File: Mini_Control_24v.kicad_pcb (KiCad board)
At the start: 2 copper layers, 130 x 100 mm, 60 parts, among them J1 Screw_Terminal_01x02, J2 Screw_Terminal_01x04, J3 Screw_Terminal_01x04, J4 Screw_Terminal_01x03, J5 Screw_Terminal_01x03, J6 ВН-20, J7 USB_B_Micro, J8 Screw_Terminal_01x02, K1 G2RL-1, K2 G2RL-1, U1 STM32F051C8Tx, U2 ISO1212, U3 ISO1212, U4 MAX3485, U5 USBLC6-2SC6, U6 FT232RL, U7 LM2596S-3.3, U8 ULN2003A

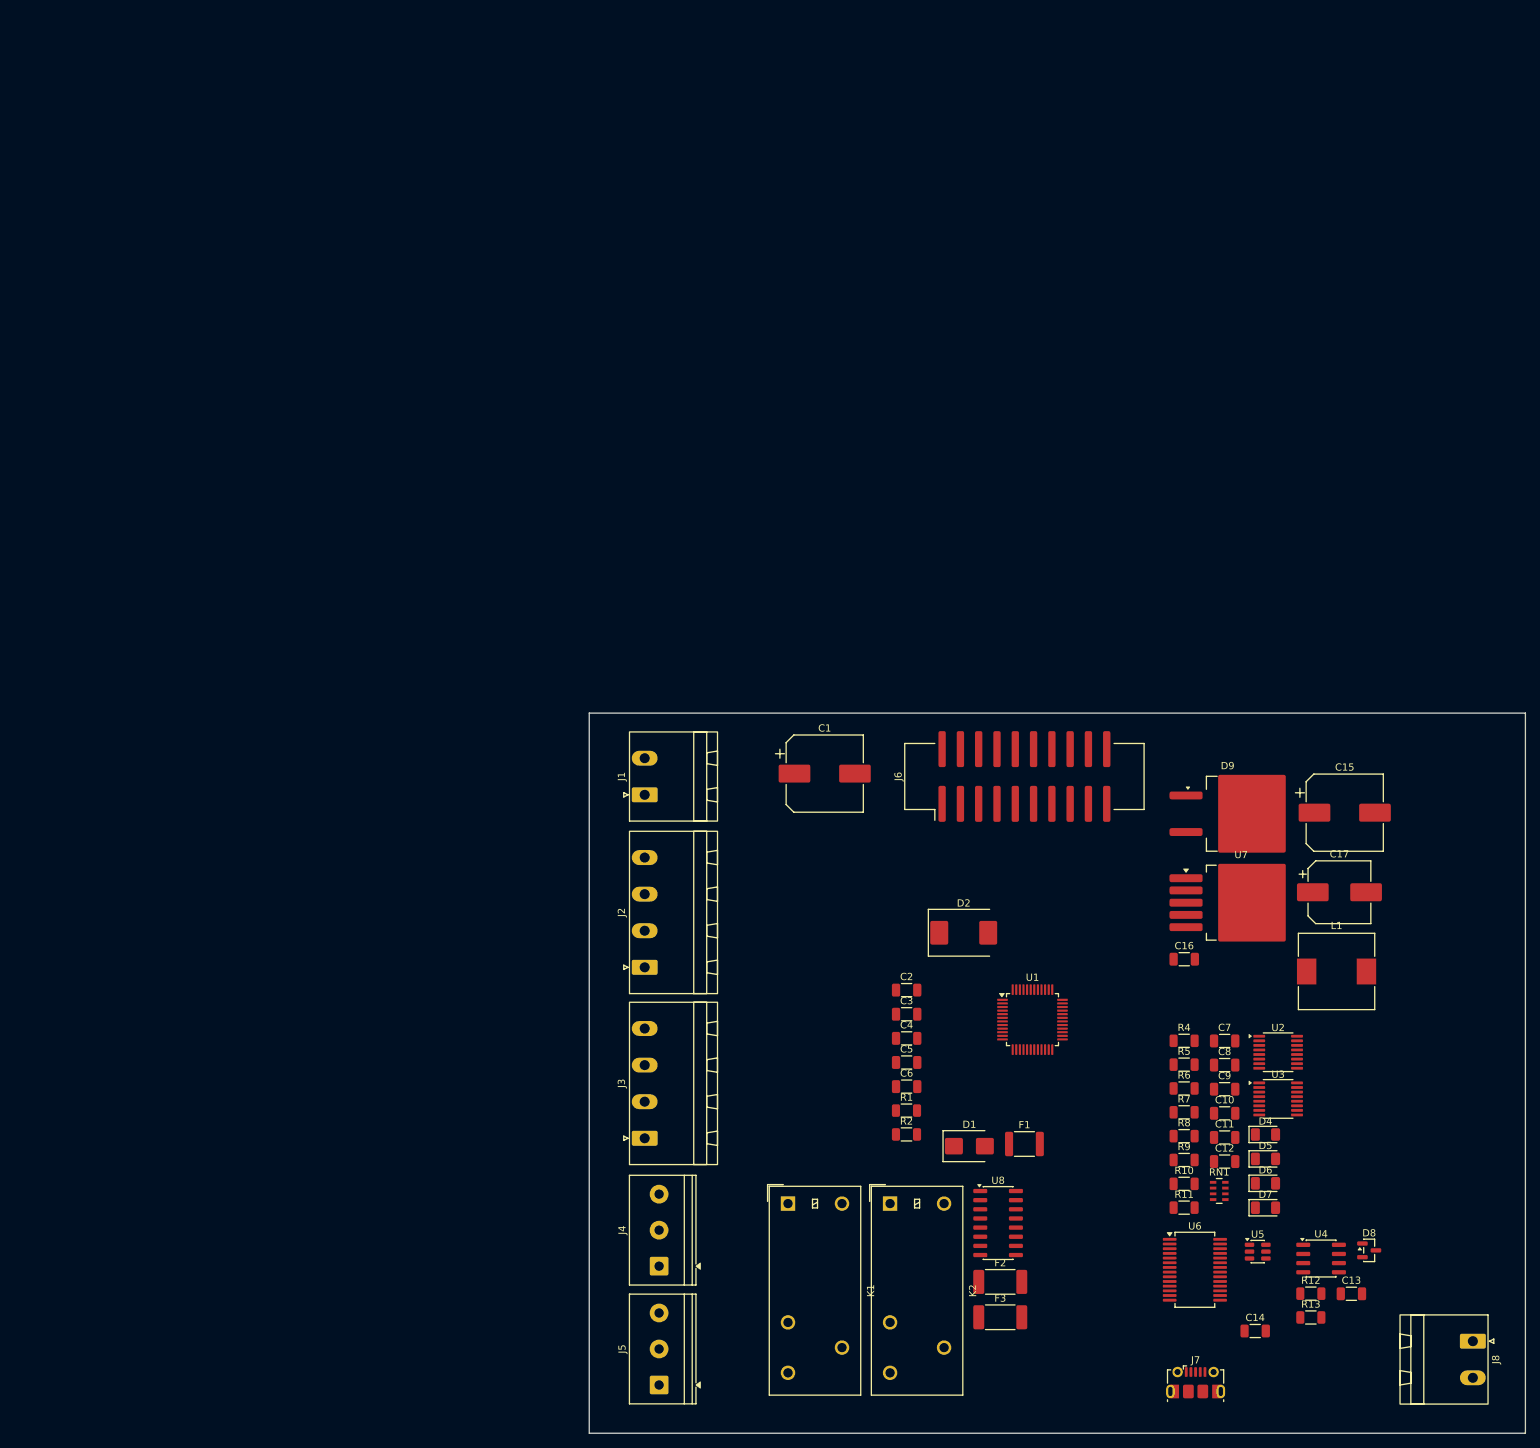
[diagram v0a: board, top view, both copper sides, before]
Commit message: Трассировка питания и цифровых входов-выходов
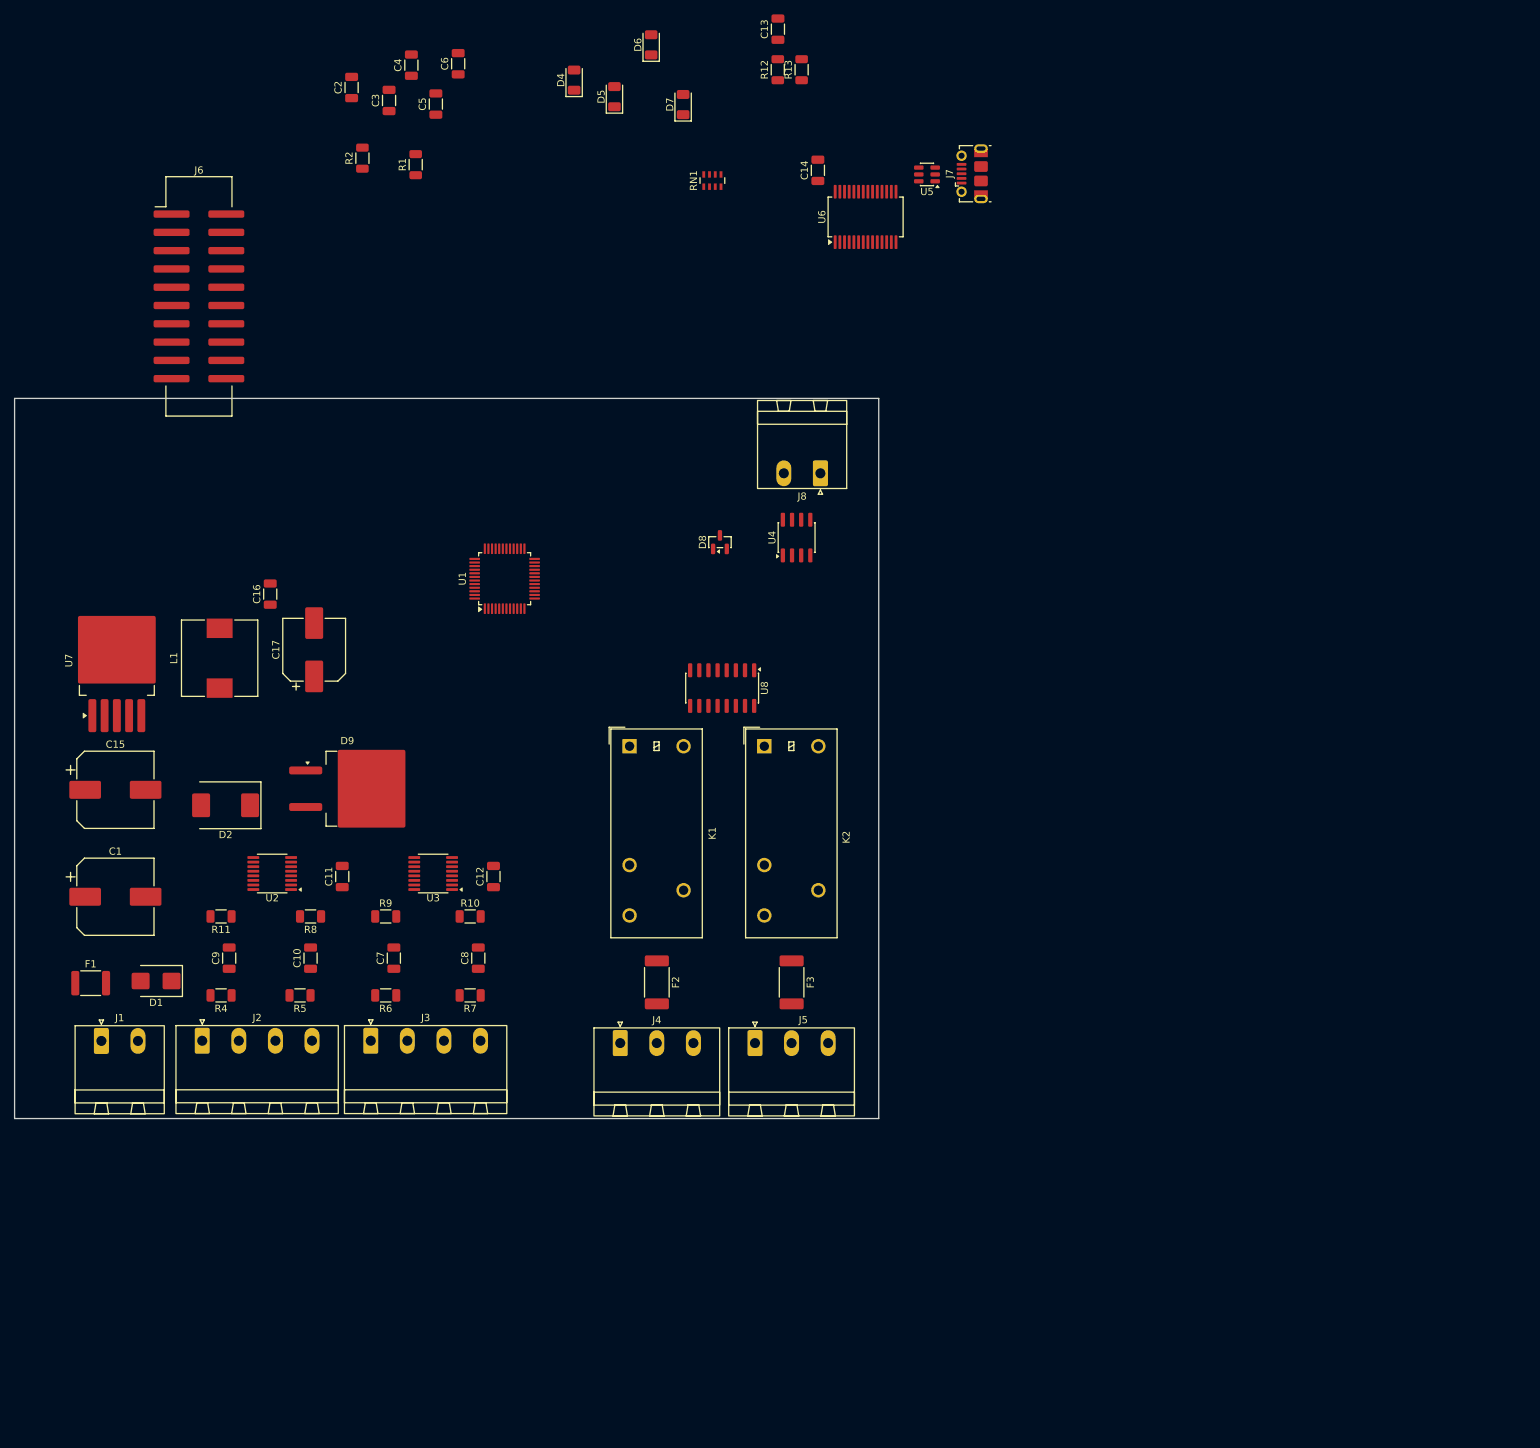
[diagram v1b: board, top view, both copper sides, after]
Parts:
- J4, J5: footprint TerminalBlock_Phoenix:TerminalBlock_Phoenix_PT-1,5-3-5.0-H_1x03_P5.00mm_Horizontal -> Connector_Phoenix_MSTB:PhoenixContact_MSTBA_2,5_3-G-5,08_1x03_P5.08mm_Horizontal
- moved C13 192.8 mm to (106.0, -51.3), turned to 90 degrees
- moved R13 187.1 mm to (109.3, -45.6), turned to 90 degrees
- moved R12 185.4 mm to (106.0, -45.6), turned to 90 degrees
- moved D6 179.6 mm to (88.4, -49.1), turned to 90 degrees
- moved D4 175.1 mm to (77.7, -44.2), turned to 90 degrees
- moved D7 173.2 mm to (92.8, -40.8), turned to 90 degrees
- moved D5 173.0 mm to (83.3, -41.9), turned to 90 degrees
- moved C14 172.2 mm to (111.5, -31.7), turned to 90 degrees
- moved C15 170.7 mm to (14.0, 54.4)
- moved J7 170.7 mm to (133.0, -31.2), turned to 90 degrees
- moved L1 161.1 mm to (28.5, 36.1), turned to 90 degrees
- moved U7 159.7 mm to (14.2, 36.4), turned to 90 degrees
- moved RN1 157.0 mm to (96.9, -30.2), turned to 90 degrees
- moved U5 156.5 mm to (126.7, -31.1), turned to 180 degrees
- moved R2 155.2 mm to (48.3, -33.4), turned to 90 degrees
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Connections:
- U8 pad 15: /Digital_Outputs/K2_A2 -> /Digital_Outputs/K1_A2
- U8 pad 16: /Digital_Outputs/K1_A2 -> /Digital_Outputs/K2_A2
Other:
- board size 130 x 100 mm -> 120 x 100 mm
